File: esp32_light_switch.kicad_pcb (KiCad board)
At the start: 2 copper layers, 26 parts, among them J1 Conn_USART0, J2 Screw_Terminal_01x02, J3 Conn_01x02, K1 G5LE-1, Q1 MMBT2222A, SW1 SW_SPST, SW2 SW_SPST, U1 ESP32-WROOM-32E, U2 PC817, U3 MIC5205-3.0YM5

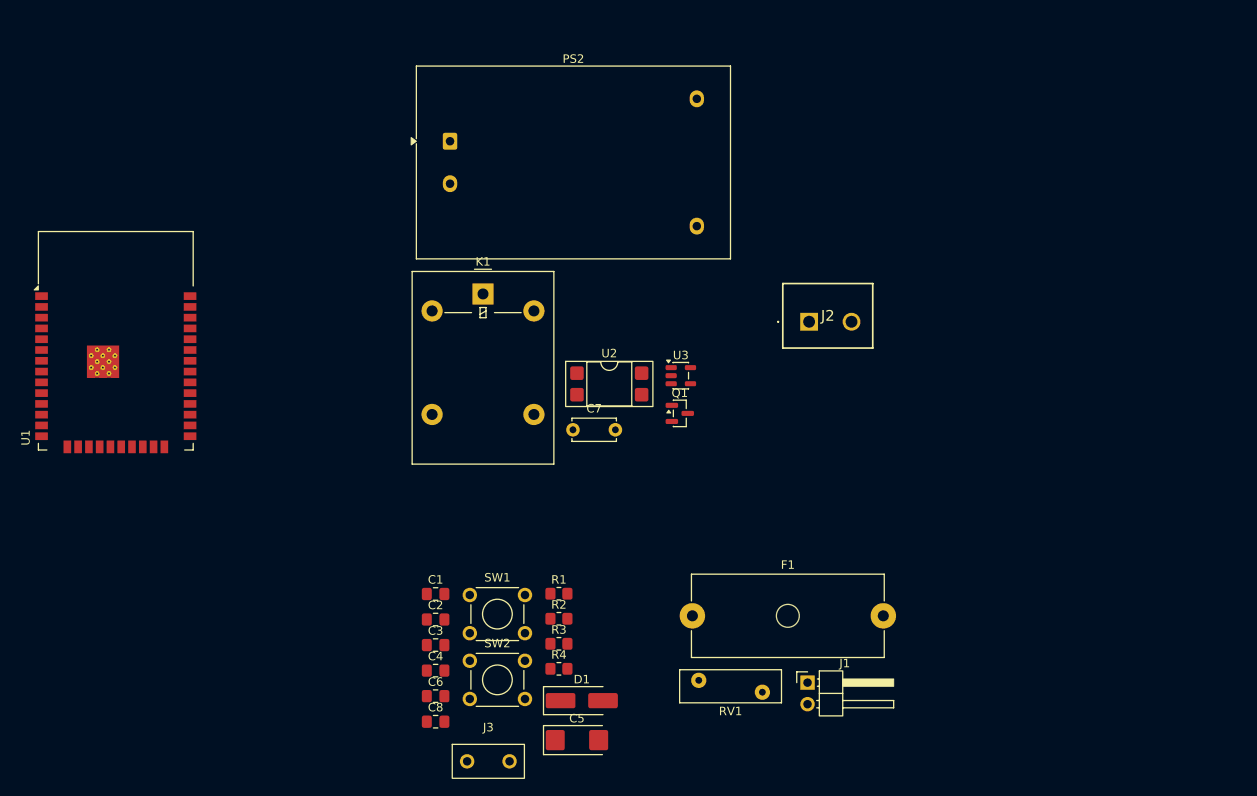
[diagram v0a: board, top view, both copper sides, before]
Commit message: refactor to use TRIAC and draw initial pcb
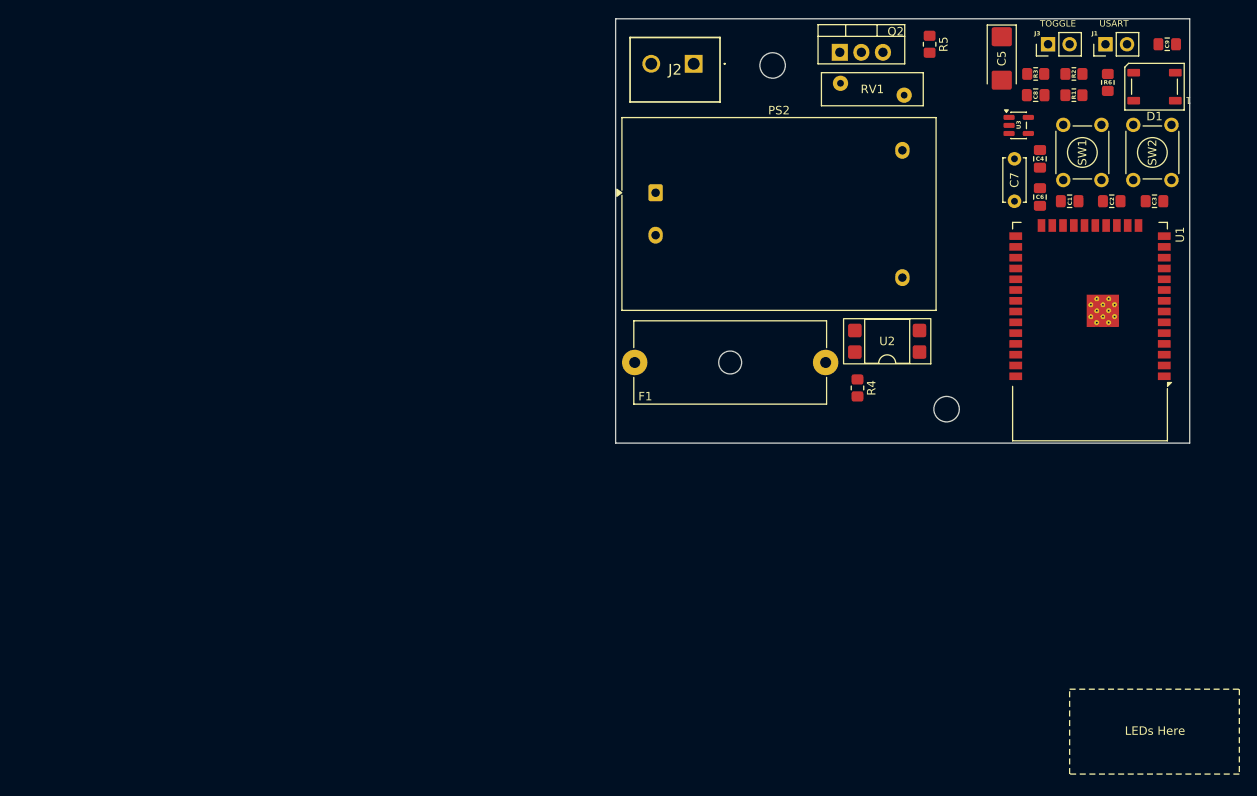
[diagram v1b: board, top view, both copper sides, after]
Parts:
- removed K1: G5LE-1, Relay_THT:Relay_SPDT_Omron-G5LE-1
- removed Q1: MMBT2222A, Package_TO_SOT_SMD:SOT-23
- added C9: 0.1uF, Capacitor_SMD:C_0805_2012Metric_Pad1.18x1.45mm_HandSolder, F.Cu at (205.5, 44.5)
- added Q2: BTB16-800B, Package_TO_SOT_THT:TO-220-3_Vertical, F.Cu at (166.9, 45.5)
- added R5: 100, Resistor_SMD:R_0805_2012Metric_Pad1.20x1.40mm_HandSolder, F.Cu at (177.5, 44.5)
- added R6: 100, Resistor_SMD:R_0805_2012Metric_Pad1.20x1.40mm_HandSolder, F.Cu at (198.5, 49.0)
- D1: value D -> WS2812B; footprint Diode_SMD:D_SMA_Handsoldering -> LED_SMD:LED_WS2812B_PLCC4_5.0x5.0mm_P3.2mm
- J1: footprint Connector_PinHeader_2.54mm:PinHeader_1x02_P2.54mm_Horizontal -> Connector_PinHeader_2.54mm:PinHeader_1x02_P2.54mm_Vertical
- J3: footprint Button_Switch_THT:Toggle BTN -> Connector_PinHeader_2.54mm:PinHeader_1x02_P2.54mm_Vertical
- moved U1 115.0 mm to (196.4, 75.4), turned to 180 degrees
- moved J3 107.2 mm to (191.5, 44.5), turned to 90 degrees
- moved C8 102.2 mm to (190.0, 50.5)
- moved C3 99.6 mm to (204.0, 63.0)
- moved D1 98.9 mm to (204.0, 49.5), turned to 180 degrees
- moved SW2 96.5 mm to (201.5, 60.5), turned to 90 degrees
- moved C5 94.6 mm to (186.0, 46.2), turned to -90 degrees
- moved C2 93.7 mm to (199.0, 63.0)
- moved C4 93.3 mm to (190.5, 58.0), turned to 90 degrees
- moved C6 92.4 mm to (190.5, 62.5), turned to 90 degrees
- moved R2 88.3 mm to (194.5, 48.0)
- moved C1 87.9 mm to (194.0, 63.0), turned to 180 degrees
- moved R3 87.6 mm to (190.0, 48.0)
- moved SW1 85.3 mm to (193.2, 60.5), turned to 90 degrees
- moved R1 84.5 mm to (194.5, 50.5)
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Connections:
- D1 pad 1: 5V -> 3V3
- D1 pad 2: Net-(D1-A) -> unconnected-(D1-DOUT-Pad2)
- U1 pad 10: unconnected-(U1-IO25-Pad10) -> LED_CTRL
- U2 pad 4: 5V -> 220VL
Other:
- board outline added: 67.7 x 50 mm
- board text added: "LEDs Here"
- board text added: "TOGGLE"
- board text added: "USART"
